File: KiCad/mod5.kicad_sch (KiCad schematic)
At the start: 51 parts, among them M10 Fan_4pin, M9 Fan_4pin, U5 ZD25Q64BSIGT

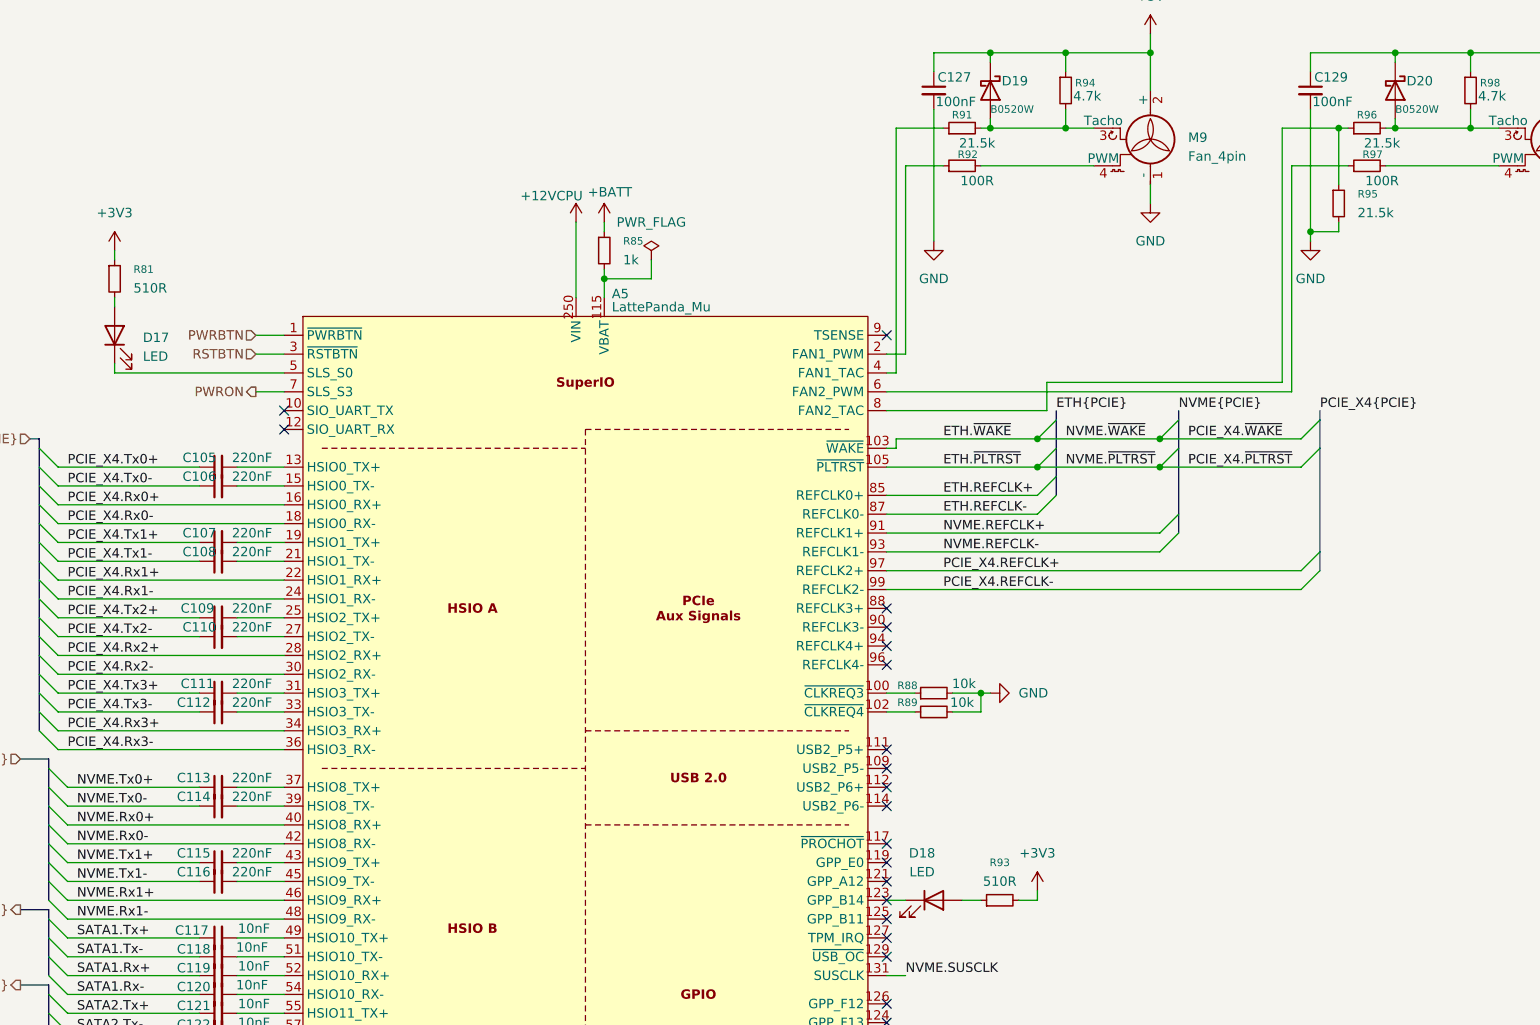
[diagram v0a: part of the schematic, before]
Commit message: Add most passive component footprints
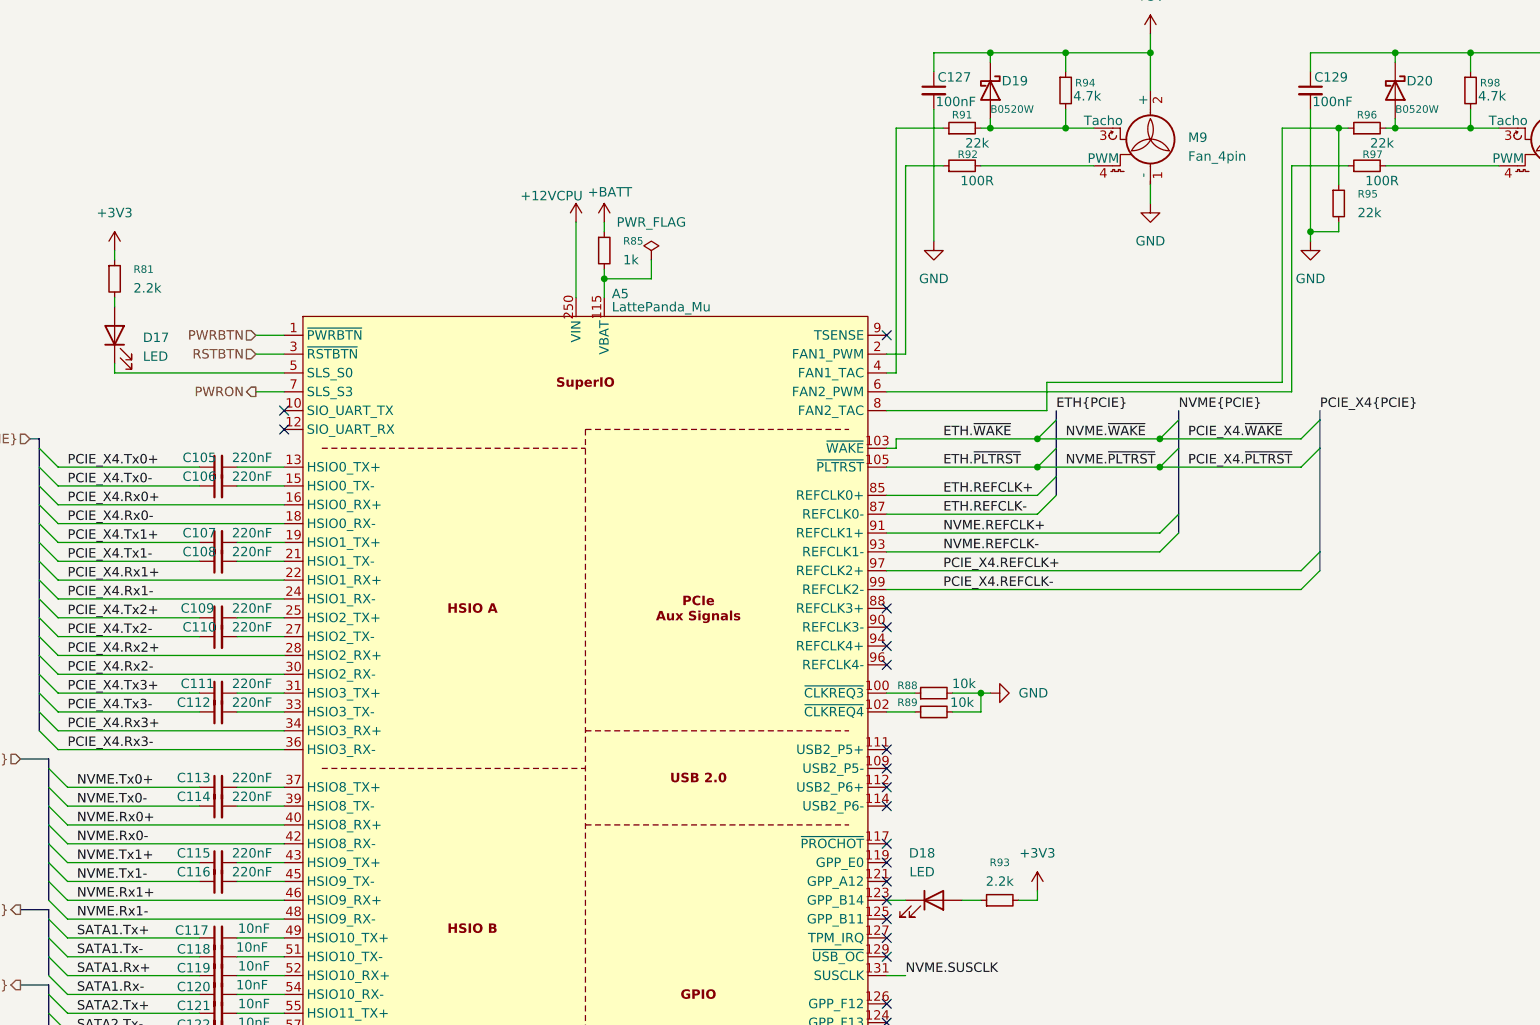
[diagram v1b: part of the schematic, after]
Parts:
- C105, C106, C107, C108, C109, C110, C111, C112, C113, C114, C115, C116, C117, C118, C119, C120, C121, C122, C123, C124, C125, C126, C127, C128: footprint Capacitor_SMD:C_0603_1608Metric -> Capacitor_SMD:C_0402_1005Metric
- D17, D18: footprint (none) -> LED_SMD:LED_0603_1608Metric
- D19, D20: footprint (none) -> Diode_SMD:D_SOD-123
- M10, M9: footprint (none) -> Connector:FanPinHeader_1x04_P2.54mm_Vertical
- R81, R93: value 510R -> 2.2k; footprint (none) -> Resistor_SMD:R_0402_1005Metric
- R82, R83, R84, R86, R87, R88, R89, R90, R92, R94, R97, R98: footprint (none) -> Resistor_SMD:R_0402_1005Metric
- R85: footprint (none) -> Resistor_SMD:R_0805_2012Metric
- R91, R95, R96: value 21.5k -> 22k; footprint (none) -> Resistor_SMD:R_0402_1005Metric
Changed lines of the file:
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@@
 			)
 		)
-		(property "Footprint" "Capacitor_SMD:C_0603_1608Metric"
+		(property "Footprint" "Capacitor_SMD:C_0402_1005Metric"
 			(at 227.33 144.78 0)
 			(effects
@@
 			)
 		)
-		(property "Footprint" ""
+		(property "Footprint" "Connector:FanPinHeader_1x04_P2.54mm_Vertical"
 			(at 353.06 48.006 0)
 			(effects
@@
 			)
 		)
-		(property "Footprint" "Capacitor_SMD:C_0603_1608Metric"
+		(property "Footprint" "Capacitor_SMD:C_0402_1005Metric"
 			(at 227.33 154.94 0)
 			(effects
@@
 			)
 		)
-		(property "Footprint" ""
+		(property "Footprint" "Resistor_SMD:R_0402_1005Metric"
 			(at 341.63 40.64 0)
 			(effects
@@
 			)
 		)
-		(property "Footprint" ""
+		(property "Footprint" "Resistor_SMD:R_0402_1005Metric"
 			(at 325.12 246.38 0)
 			(effects
@@
 			)
 		)
-		(property "Footprint" ""
+		(property "Footprint" "Resistor_SMD:R_0402_1005Metric"
 			(at 323.85 121.92 0)
 			(effects
@@
 			)
 		)
-		(property "Footprint" ""
+		(property "Footprint" "Resistor_SMD:R_0402_1005Metric"
 			(at 227.33 259.08 0)
 			(effects
@@
 			)
 		)
-		(property "Footprint" "Capacitor_SMD:C_0603_1608Metric"
+		(property "Footprint" "Capacitor_SMD:C_0402_1005Metric"
 			(at 227.33 165.1 0)
 			(effects
@@
 			)
 		)
-		(property "Value" "21.5k"
+		(property "Value" "22k"
 			(at 329.692 47.752 90)
 			(effects
@@
 			)
 		)
-		(property "Footprint" ""
+		(property "Footprint" "Resistor_SMD:R_0402_1005Metric"
 			(at 327.66 45.72 0)
 			(effects
@@
 			)
 		)
-		(property "Footprint" ""
+		(property "Footprint" "Resistor_SMD:R_0402_1005Metric"
 			(at 323.85 124.46 0)
 			(effects
@@
 			)
 		)
-		(property "Footprint" "Capacitor_SMD:C_0603_1608Metric"
+		(property "Footprint" "Capacitor_SMD:C_0402_1005Metric"
 			(at 227.33 137.16 0)
 			(effects
@@
 			)
 		)
-		(property "Footprint" ""
+		(property "Footprint" "Resistor_SMD:R_0402_1005Metric"
 			(at 396.24 40.64 0)
 			(effects
@@
 			)
 		)
-		(property "Footprint" "Capacitor_SMD:C_0603_1608Metric"
+		(property "Footprint" "Capacitor_SMD:C_0402_1005Metric"
 			(at 227.33 167.64 0)
 			(effects
@@
 			)
 		)
-		(property "Value" "21.5k"
+		(property "Value" "22k"
 			(at 384.302 47.752 90)
 			(effects
@@
 			)
 		)
-		(property "Footprint" ""
+		(property "Footprint" "Resistor_SMD:R_0402_1005Metric"
 			(at 382.27 45.72 0)
 			(effects
@@
 			)
 		)
-		(property "Footprint" ""
+		(property "Footprint" "Resistor_SMD:R_0805_2012Metric"
 			(at 279.4 62.23 0)
 			(effects
@@
 			)
 		)
-		(property "Footprint" "Capacitor_SMD:C_0603_1608Metric"
+		(property "Footprint" "Capacitor_SMD:C_0402_1005Metric"
 			(at 227.33 160.02 0)
 			(effects
@@
 			)
 		)
-		(property "Footprint" ""
+		(property "Footprint" "Connector:FanPinHeader_1x04_P2.54mm_Vertical"
 			(at 407.67 48.006 0)
 			(effects
@@
 			)
 		)
-		(property "Footprint" "Capacitor_SMD:C_0603_1608Metric"
+		(property "Footprint" "Capacitor_SMD:C_0402_1005Metric"
 			(at 227.33 177.8 0)
 			(effects
@@
 			)
 		)
-		(property "Footprint" ""
+		(property "Footprint" "Resistor_SMD:R_0402_1005Metric"
 			(at 327.66 50.8 0)
 			(effects
@@
 			)
 		)
-		(property "Value" "510R"
+		(property "Value" "2.2k"
 			(at 215.9 67.3099 0)
 			(effects
@@
 			)
 		)
-		(property "Footprint" ""
+		(property "Footprint" "Resistor_SMD:R_0402_1005Metric"
 			(at 213.36 66.04 0)
 			(effects
@@
 			)
 		)
-		(property "Footprint" ""
+		(property "Footprint" "Diode_SMD:D_SOD-123"
 			(at 386.08 40.64 0)
 			(effects
@@
 			)
 		)
-		(property "Footprint" ""
+		(property "Footprint" "Resistor_SMD:R_0402_1005Metric"
 			(at 227.33 297.18 0)
 			(effects
@@
 			)
 		)
-		(property "Footprint" "Capacitor_SMD:C_0603_1608Metric"
+		(property "Footprint" "Capacitor_SMD:C_0402_1005Metric"
 			(at 342.9 242.57 0)
 			(effects
@@
 			)
 		)
-		(property "Footprint" "Capacitor_SMD:C_0603_1608Metric"
+		(property "Footprint" "Capacitor_SMD:C_0402_1005Metric"
 			(at 227.33 170.18 0)
 			(effects
@@
 			)
 		)
-		(property "Footprint" "Capacitor_SMD:C_0603_1608Metric"
+		(property "Footprint" "Capacitor_SMD:C_0402_1005Metric"
 			(at 227.33 111.76 0)
 			(effects
@@
 			)
 		)
-		(property "Footprint" "Capacitor_SMD:C_0603_1608Metric"
+		(property "Footprint" "Capacitor_SMD:C_0402_1005Metric"
 			(at 227.33 121.92 0)
 			(effects
@@
 			)
 		)
-		(property "Footprint" ""
+		(property "Footprint" "LED_SMD:LED_0603_1608Metric"
 			(at 323.85 149.86 0)
 			(effects
@@
 			)
 		)
-		(property "Footprint" ""
+		(property "Footprint" "Diode_SMD:D_SOD-123"
 			(at 331.47 40.64 0)
 			(effects
@@
 			)
 		)
-		(property "Footprint" "Capacitor_SMD:C_0603_1608Metric"
+		(property "Footprint" "Capacitor_SMD:C_0402_1005Metric"
 			(at 227.33 147.32 0)
 			(effects
@@
 			)
 		)
-		(property "Value" "21.5k"
+		(property "Value" "22k"
 			(at 381 57.1499 0)
 			(effects
@@
 			)
 		)
-		(property "Footprint" ""
+		(property "Footprint" "Resistor_SMD:R_0402_1005Metric"
 			(at 378.46 55.88 0)
 			(effects
@@
 			)
 		)
-		(property "Value" "510R"
+		(property "Value" "2.2k"
 			(at 332.74 147.32 90)
 			(effects
@@
 			)
 		)
-		(property "Footprint" ""
+		(property "Footprint" "Resistor_SMD:R_0402_1005Metric"
 			(at 332.74 149.86 0)
 			(effects
@@
 			)
 		)
-		(property "Footprint" "Capacitor_SMD:C_0603_1608Metric"
+		(property "Footprint" "Capacitor_SMD:C_0402_1005Metric"
 			(at 227.33 91.44 0)
 			(effects
@@
 			)
 		)
-		(property "Footprint" "Capacitor_SMD:C_0603_1608Metric"
+		(property "Footprint" "Capacitor_SMD:C_0402_1005Metric"
 			(at 227.33 172.72 0)
 			(effects
@@
 			)
 		)
-		(property "Footprint" "Capacitor_SMD:C_0603_1608Metric"
+		(property "Footprint" "Capacitor_SMD:C_0402_1005Metric"
 			(at 227.33 157.48 0)
 			(effects
@@
 			)
 		)
-		(property "Footprint" "Capacitor_SMD:C_0603_1608Metric"
+		(property "Footprint" "Capacitor_SMD:C_0402_1005Metric"
 			(at 227.33 162.56 0)
 			(effects
@@
 			)
 		)
-		(property "Footprint" "Capacitor_SMD:C_0603_1608Metric"
+		(property "Footprint" "Capacitor_SMD:C_0402_1005Metric"
 			(at 227.33 104.14 0)
 			(effects
@@
 			)
 		)
-		(property "Footprint" ""
+		(property "Footprint" "Resistor_SMD:R_0402_1005Metric"
 			(at 227.33 220.98 0)
 			(effects
@@
 			)
 		)
-		(property "Footprint" ""
+		(property "Footprint" "Resistor_SMD:R_0402_1005Metric"
 			(at 320.04 273.05 0)
 			(effects
@@
 			)
 		)
-		(property "Footprint" "Capacitor_SMD:C_0603_1608Metric"
+		(property "Footprint" "Capacitor_SMD:C_0402_1005Metric"
 			(at 227.33 180.34 0)
 			(effects
@@
 			)
 		)
-		(property "Footprint" "Capacitor_SMD:C_0603_1608Metric"
+		(property "Footprint" "Capacitor_SMD:C_0402_1005Metric"
 			(at 227.33 101.6 0)
 			(effects
@@
 			)
 		)
-		(property "Footprint" ""
+		(property "Footprint" "Resistor_SMD:R_0402_1005Metric"
 			(at 382.27 50.8 0)
 			(effects
@@
 			)
 		)
-		(property "Footprint" "Capacitor_SMD:C_0603_1608Metric"
+		(property "Footprint" "Capacitor_SMD:C_0402_1005Metric"
 			(at 323.85 40.64 0)
 			(effects
@@
 			)
 		)
-		(property "Footprint" ""
+		(property "Footprint" "Resistor_SMD:R_0402_1005Metric"
 			(at 320.04 246.38 0)
 			(effects
@@
 			)
 		)
-		(property "Footprint" "Capacitor_SMD:C_0603_1608Metric"
+		(property "Footprint" "Capacitor_SMD:C_0402_1005Metric"
 			(at 227.33 114.3 0)
 			(effects
@@
 			)
 		)
-		(property "Footprint" ""
+		(property "Footprint" "LED_SMD:LED_0603_1608Metric"
 			(at 213.36 73.66 0)
 			(effects
@@
 			)
 		)
-		(property "Footprint" "Capacitor_SMD:C_0603_1608Metric"
+		(property "Footprint" "Capacitor_SMD:C_0402_1005Metric"
 			(at 227.33 93.98 0)
 			(effects
@@
 			)
 		)
-		(property "Footprint" "Capacitor_SMD:C_0603_1608Metric"
+		(property "Footprint" "Capacitor_SMD:C_0402_1005Metric"
 			(at 227.33 134.62 0)
 			(effects
@@
 			)
 		)
-		(property "Footprint" "Capacitor_SMD:C_0603_1608Metric"
+		(property "Footprint" "Capacitor_SMD:C_0402_1005Metric"
 			(at 227.33 124.46 0)
 			(effects

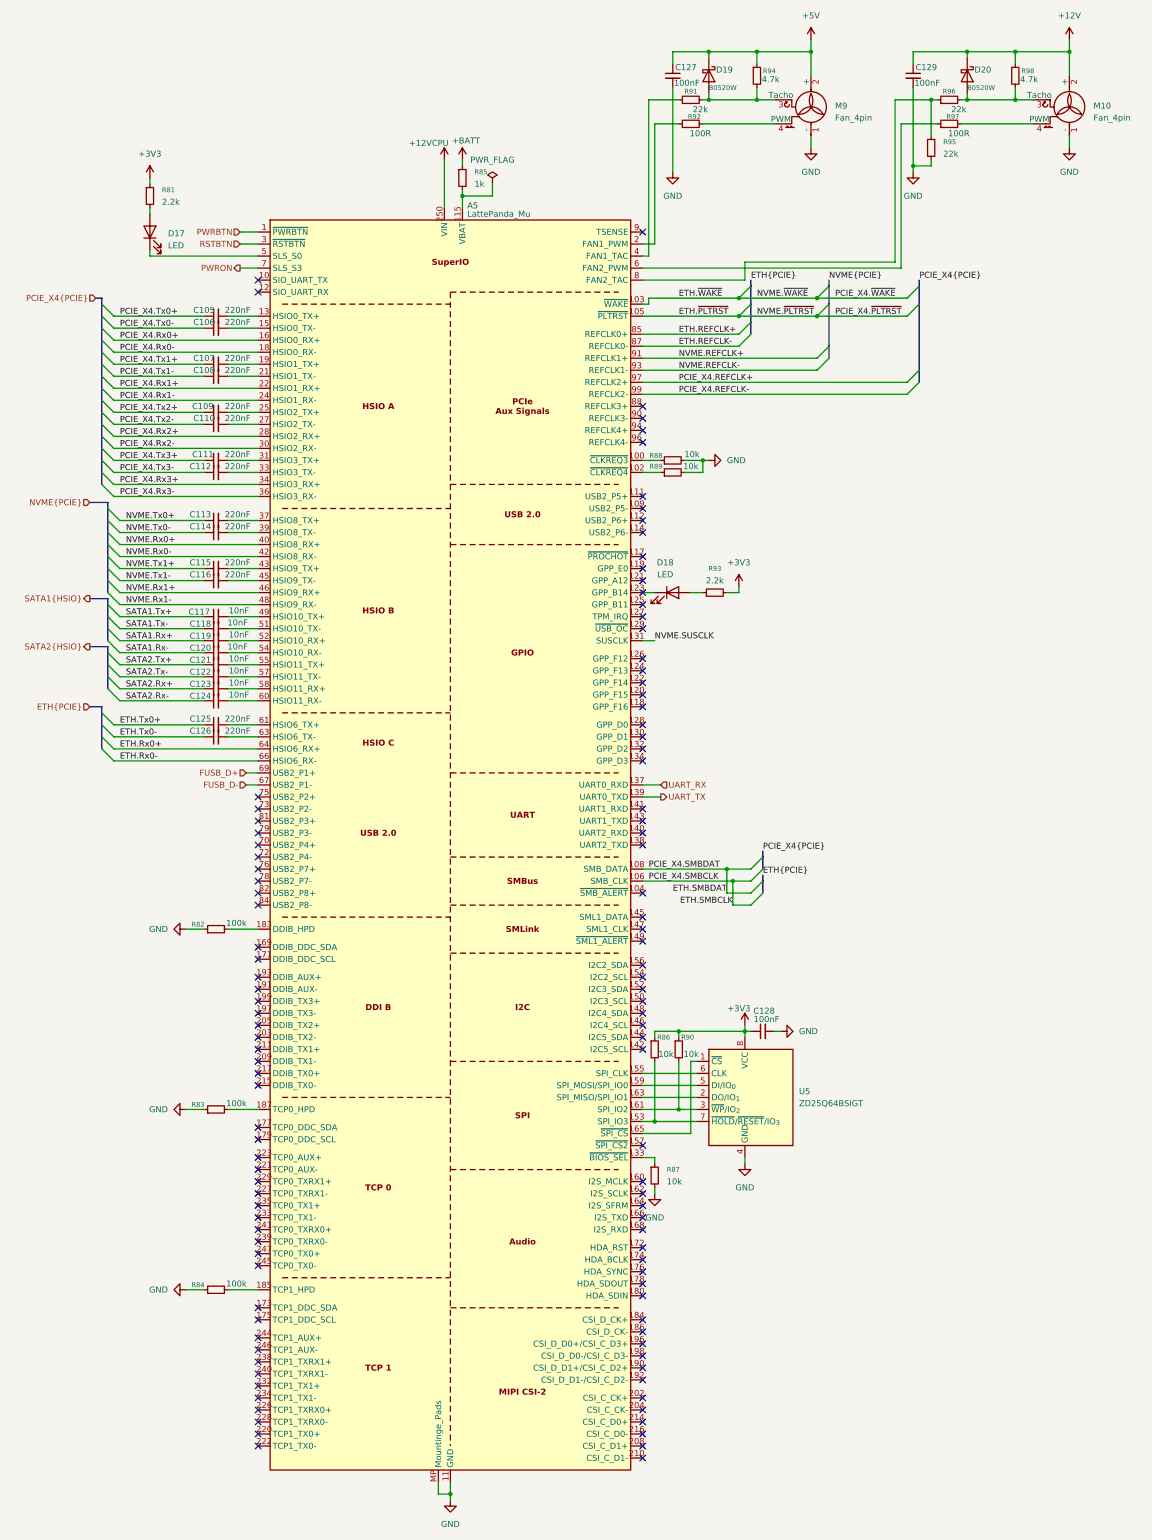
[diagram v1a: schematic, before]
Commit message: Finish fixing footprints
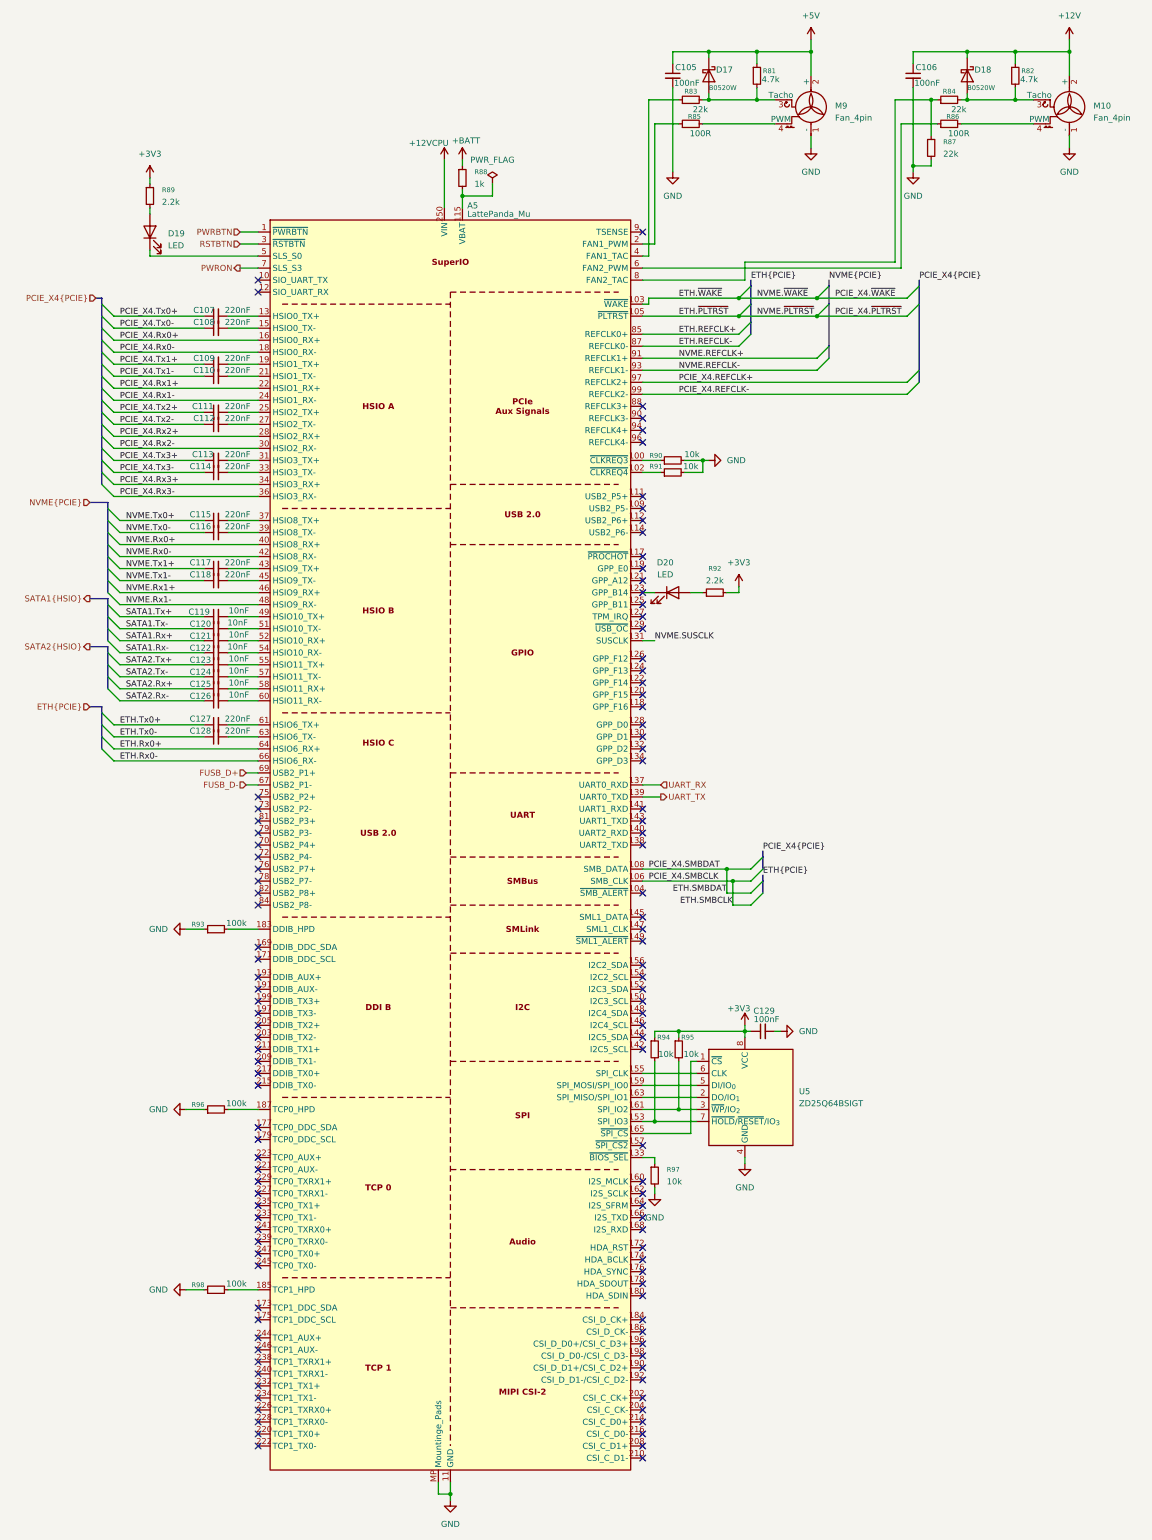
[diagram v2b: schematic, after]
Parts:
- renumbered C127 to C105, C129 to C106, C105 to C107, C106 to C108, C107 to C109, C108 to C110, C109 to C111, C110 to C112, C111 to C113, C112 to C114, C113 to C115, C114 to C116, C115 to C117, C116 to C118, C117 to C119, C118 to C120, C119 to C121, C120 to C122, C121 to C123, C122 to C124, C123 to C125, C124 to C126, C125 to C127, C126 to C128, C128 to C129, D19 to D17, D20 to D18, D17 to D19, D18 to D20, R94 to R81, R98 to R82, R91 to R83, R96 to R84, R92 to R85, R97 to R86, R95 to R87, R85 to R88, R81 to R89, R88 to R90, R89 to R91, R93 to R92, R82 to R93, R86 to R94, R90 to R95, R83 to R96, R87 to R97, R84 to R98
